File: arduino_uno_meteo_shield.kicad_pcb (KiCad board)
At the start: 2 copper layers, 13 parts

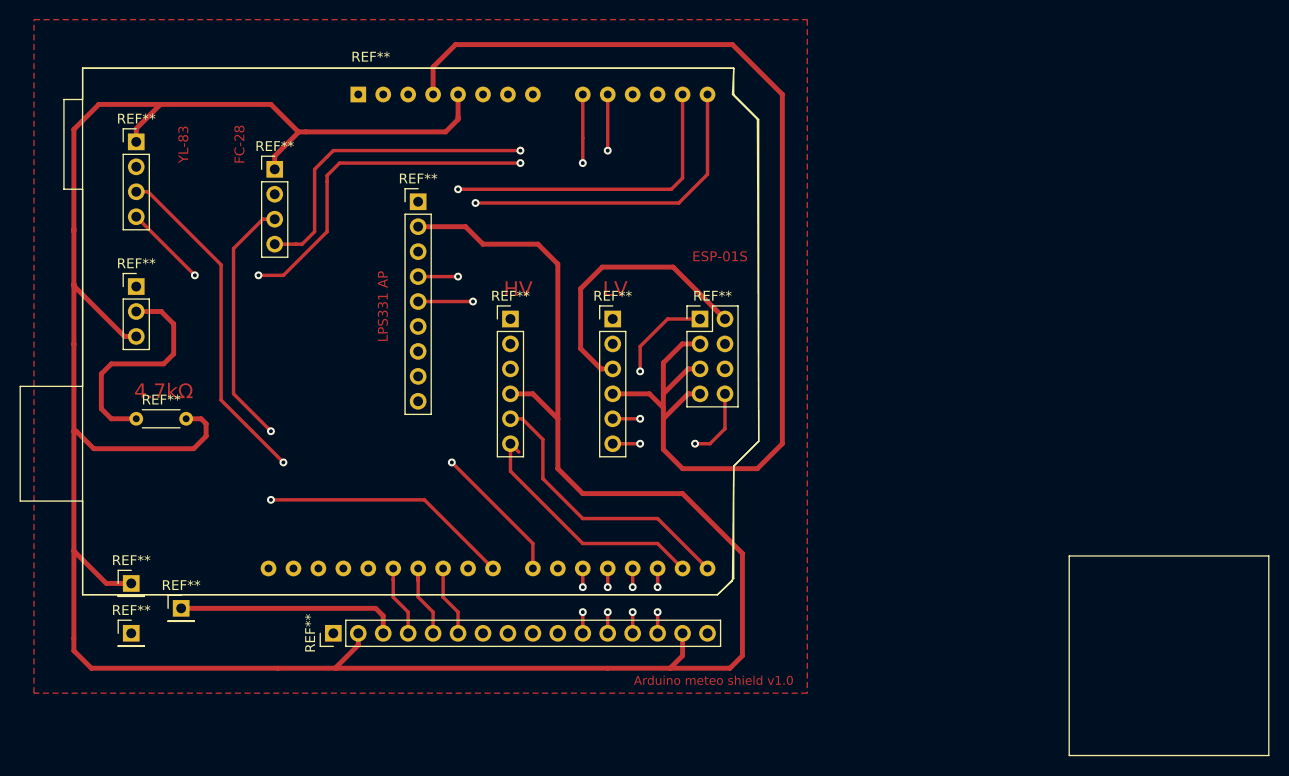
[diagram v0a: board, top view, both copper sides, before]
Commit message: make path wider
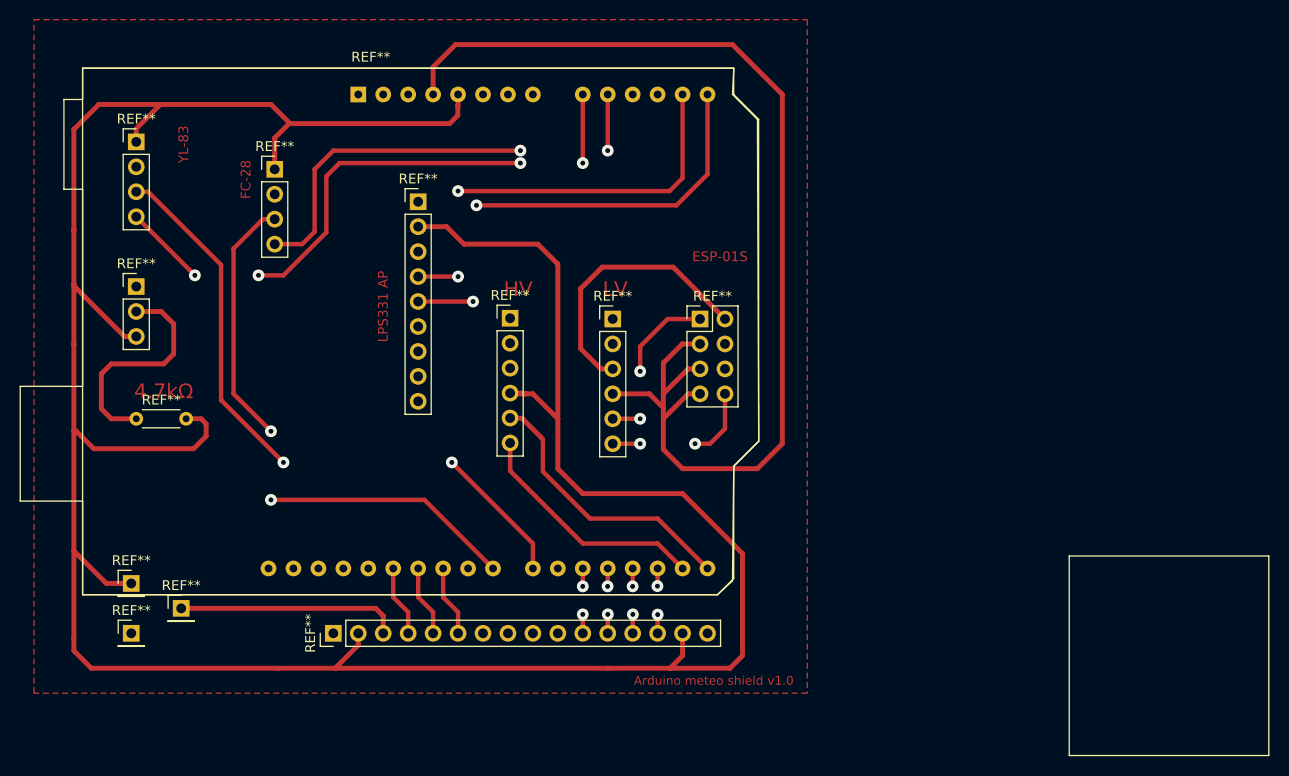
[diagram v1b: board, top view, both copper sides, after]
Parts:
- moved REF** 0.08 mm to (157.7, 88.8)
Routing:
- net (no net): track 870.0 -> 894.8 mm

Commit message: improving connections and add DTH11
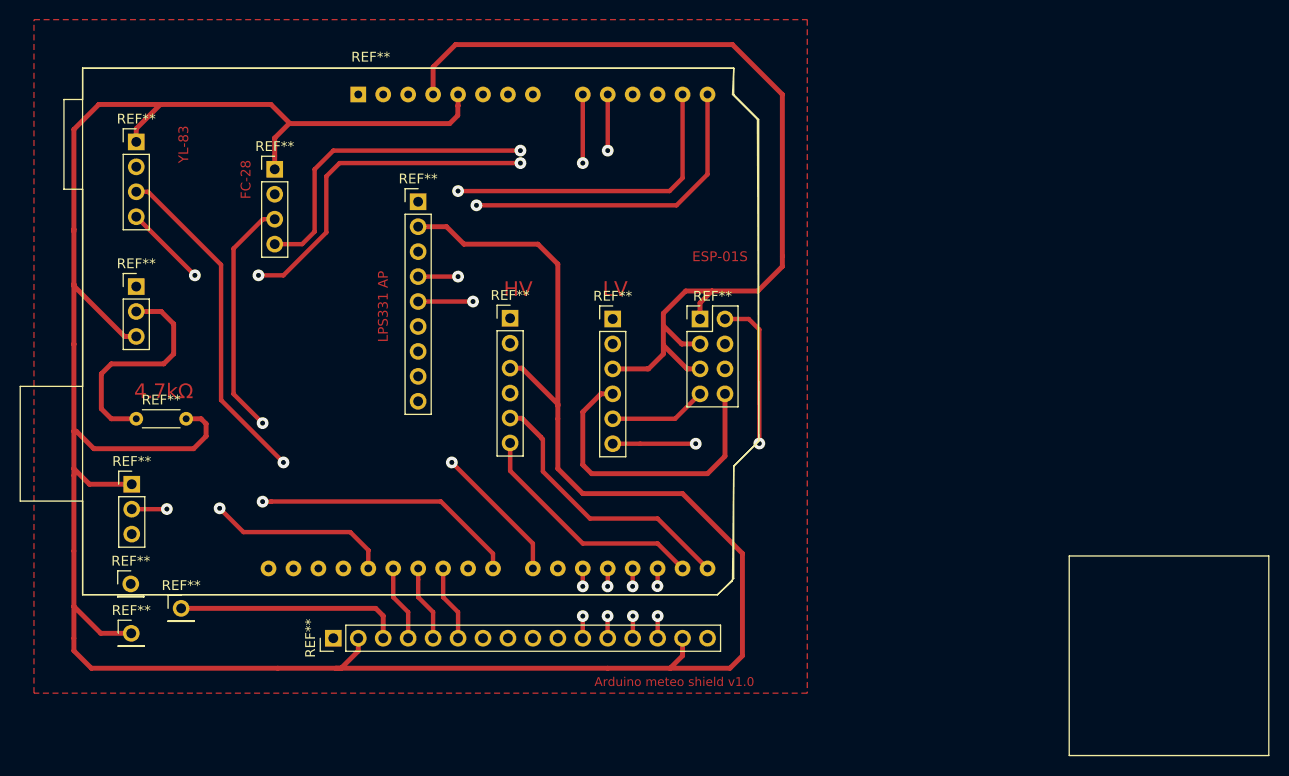
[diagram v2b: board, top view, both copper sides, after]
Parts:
- added REF**: PinHeader_1x03_P2.54mm_Vertical, Connector_PinHeader_2.54mm:PinHeader_1x03_P2.54mm_Vertical, F.Cu at (119.2, 105.7)
- moved REF** 0.50 mm to (139.7, 121.4)
- moved REF** 0.07 mm to (119.1, 115.9)
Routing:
- net (no net): track 894.8 -> 913.4 mm

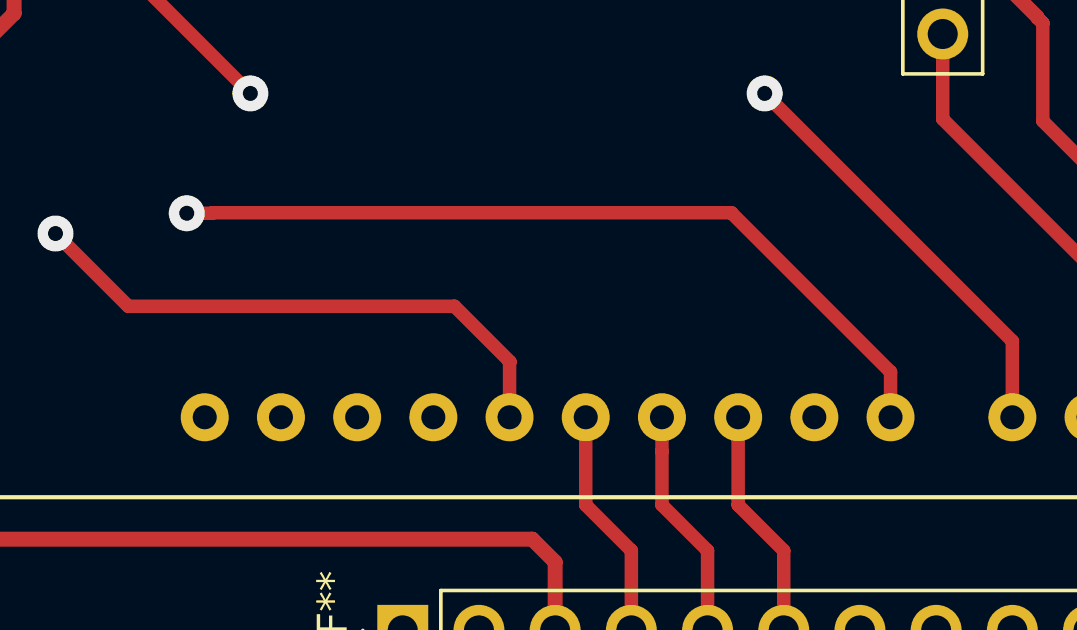
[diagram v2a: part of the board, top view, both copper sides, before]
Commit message: add holes for attachment
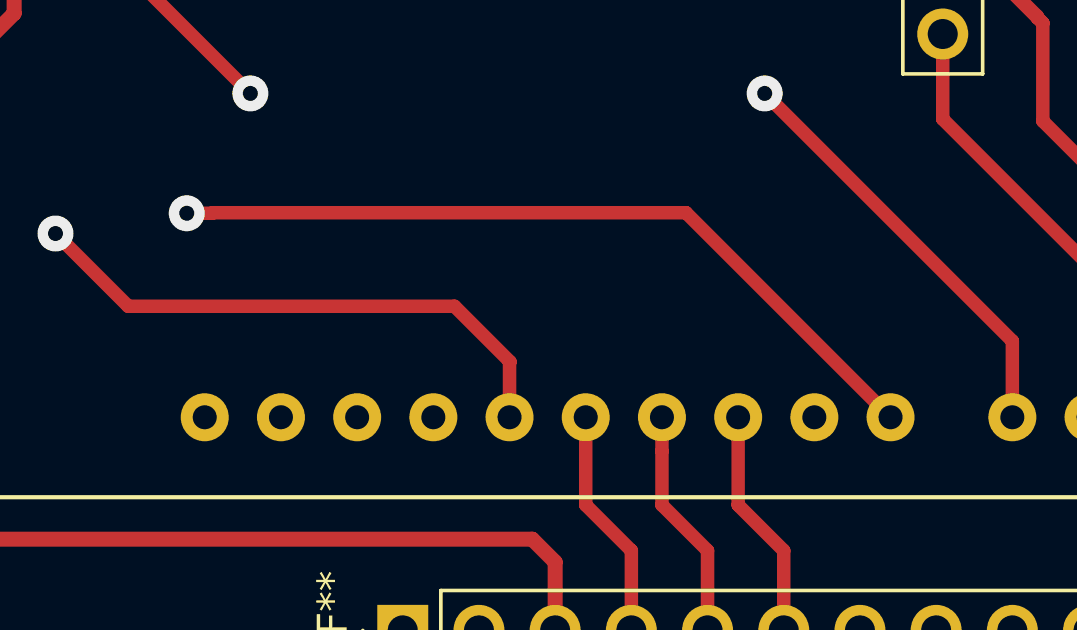
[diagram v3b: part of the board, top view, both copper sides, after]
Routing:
- net (no net): track 913.4 -> 912.5 mm
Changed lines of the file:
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@@
     (thickness 1.6)
     (drawings 21)
-    (tracks 241)
+    (tracks 240)
     (zones 0)
     (modules 14)
@@
   (segment (start 133.731 78.74) (end 132.528919 78.74) (width 0.45) (layer F.Cu) (net 0))
   (segment (start 132.528919 78.74) (end 129.54 81.728919) (width 0.45) (layer F.Cu) (net 0))
-  (segment (start 133.348528 107.5) (end 132.5 107.5) (width 0.45) (layer F.Cu) (net 0))
-  (segment (start 133.366028 107.4825) (end 133.348528 107.5) (width 0.45) (layer F.Cu) (net 0))
-  (segment (start 150.6525 107.4825) (end 133.366028 107.4825) (width 0.45) (layer F.Cu) (net 0))
-  (segment (start 155.96 114.3) (end 155.96 112.79) (width 0.45) (layer F.Cu) (net 0))
-  (segment (start 155.96 112.79) (end 150.6525 107.4825) (width 0.45) (layer F.Cu) (net 0))
+  (segment (start 133.366028 107.4825) (end 149.1425 107.4825) (width 0.45) (layer F.Cu) (net 0))
+  (segment (start 133.348528 107.5) (end 133.366028 107.4825) (width 0.45) (layer F.Cu) (net 0))
+  (segment (start 132.5 107.5) (end 133.348528 107.5) (width 0.45) (layer F.Cu) (net 0))
+  (segment (start 149.1425 107.4825) (end 155.96 114.3) (width 0.45) (layer F.Cu) (net 0))
   (zone (net 0) (net_name "") (layer F.Cu) (hatch edge 0.508)
     (connect_pads (clearance 0.508))
@@
       )
     )
+  )
+  (zone (net 0) (net_name "") (layer F.Cu) (hatch edge 0.508)
+    (connect_pads (clearance 0.508))
+    (min_thickness 0.254)
+    (keepout (tracks not_allowed) (vias not_allowed) (copperpour not_allowed))
+    (fill (arc_segments 32) (thermal_gap 0.508) (thermal_bridge_width 0.508))
+    (polygon
+      (pts
+        (xy 185.42 58.42) (xy 187.96 58.42) (xy 187.96 60.96) (xy 185.42 60.96)
+      )
+    )
+  )
+  (zone (net 0) (net_name "") (layer F.Cu) (hatch edge 0.508)
+    (connect_pads (clearance 0.508))
+    (min_thickness 0.254)
+    (keepout (tracks not_allowed) (vias not_allowed) (copperpour not_allowed))
+    (fill (arc_segments 32) (thermal_gap 0.508) (thermal_bridge_width 0.508))
+    (polygon
+      (pts
+        (xy 111.76 60.96) (xy 109.22 60.96) (xy 109.22 58.42) (xy 111.76 58.42)
+      )
+    )
+  )
+  (zone (net 0) (net_name "") (layer F.Cu) (hatch edge 0.508)
+    (connect_pads (clearance 0.508))
+    (min_thickness 0.254)
+    (keepout (tracks not_allowed) (vias not_allowed) (copperpour not_allowed))
+    (fill (arc_segments 32) (thermal_gap 0.508) (thermal_bridge_width 0.508))
+    (polygon
+      (pts
+        (xy 109.22 124.46) (xy 111.76 124.46) (xy 111.76 127) (xy 109.22 127)
+      )
+    )
+  )
+  (zone (net 0) (net_name "") (layer F.Cu) (hatch edge 0.508)
+    (connect_pads (clearance 0.508))
+    (min_thickness 0.254)
+    (keepout (tracks not_allowed) (vias not_allowed) (copperpour not_allowed))
+    (fill (arc_segments 32) (thermal_gap 0.508) (thermal_bridge_width 0.508))
+    (polygon
+      (pts
+        (xy 185.42 127) (xy 185.42 124.46) (xy 187.96 124.46) (xy 187.96 127)
+      )
+    )

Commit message: mirror fix
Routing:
- net (no net): track 912.5 -> 938.4 mm, vias 26 -> 32
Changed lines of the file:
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@@
     (thickness 1.6)
     (drawings 21)
-    (tracks 240)
+    (tracks 251)
     (zones 0)
     (modules 14)
@@
   (segment (start 133.731 72.31) (end 133.731 73.66) (width 0.5) (layer F.Cu) (net 0))
   (segment (start 133.35 67.056) (end 122.094 67.056) (width 0.5) (layer F.Cu) (net 0))
-  (segment (start 151.765 103.505) (end 151.765 103.505) (width 0.35) (layer F.Cu) (net 0))
-  (via (at 151.765 103.505) (size 1.2) (drill 0.5) (layers F.Cu B.Cu) (net 0))
-  (segment (start 134.62 103.505) (end 134.62 103.505) (width 0.35) (layer F.Cu) (net 0))
-  (via (at 134.62 103.505) (size 1.2) (drill 0.5) (layers F.Cu B.Cu) (net 0))
+  (via (at 140.716 104.14) (size 1.2) (drill 0.5) (layers F.Cu B.Cu) (net 0))
+  (via (at 134.62 104.14) (size 1.2) (drill 0.5) (layers F.Cu B.Cu) (net 0))
   (via (at 132.5 99.5) (size 1.2) (drill 0.5) (layers F.Cu B.Cu) (net 0))
   (via (at 132.5 107.5) (size 1.2) (drill 0.5) (layers F.Cu B.Cu) (net 0))
@@
   (via (at 170.2 119.15) (size 1.2) (drill 0.5) (layers F.Cu B.Cu) (net 0))
   (via (at 172.725 119.15) (size 1.2) (drill 0.5) (layers F.Cu B.Cu) (net 0))
-  (segment (start 148.34 114.3) (end 148.34 115.574) (width 0.35) (layer F.Cu) (net 0))
-  (segment (start 148.34 117.225) (end 148.34 115.574) (width 0.35) (layer F.Cu) (net 0))
   (segment (start 145.8 117.225) (end 145.8 115.43137) (width 0.35) (layer F.Cu) (net 0))
   (segment (start 158.75 71.755) (end 158.75 71.755) (width 0.35) (layer F.Cu) (net 0))
@@
   (via (at 165.1 73.025) (size 1.2) (drill 0.5) (layers F.Cu B.Cu) (net 0))
   (via (at 167.64 71.755) (size 1.2) (drill 0.5) (layers F.Cu B.Cu) (net 0))
-  (segment (start 119.634 75.946) (end 120.836081 75.946) (width 0.45) (layer F.Cu) (net 0))
-  (segment (start 120.836081 75.946) (end 128.27 83.379919) (width 0.45) (layer F.Cu) (net 0))
-  (segment (start 128.27 83.379919) (end 128.27 97.155) (width 0.45) (layer F.Cu) (net 0))
-  (segment (start 128.27 97.155) (end 134.62 103.505) (width 0.45) (layer F.Cu) (net 0))
   (segment (start 160.850541 100.93346) (end 160.850541 100.974459) (width 0.45) (layer F.Cu) (net 0))
   (segment (start 158.902081 98.985) (end 160.850541 100.93346) (width 0.45) (layer F.Cu) (net 0))
@@
   (segment (start 161.036 104.426) (end 165.83 109.22) (width 0.45) (layer F.Cu) (net 0))
   (segment (start 165.83 109.22) (end 172.72 109.22) (width 0.45) (layer F.Cu) (net 0))
-  (segment (start 151.765 103.505) (end 160.02 111.76) (width 0.45) (layer F.Cu) (net 0))
   (segment (start 160.02 111.76) (end 160.02 114.3) (width 0.45) (layer F.Cu) (net 0))
   (segment (start 145.8 114.3) (end 145.8 117.225) (width 0.45) (layer F.Cu) (net 0))
   (segment (start 147.32 118.745) (end 145.8 117.225) (width 0.45) (layer F.Cu) (net 0))
   (segment (start 147.32 120.904) (end 147.32 118.745) (width 0.45) (layer F.Cu) (net 0))
-  (segment (start 148.34 115.43137) (end 148.34 117.225) (width 0.45) (layer F.Cu) (net 0))
-  (segment (start 148.34 114.3) (end 148.34 115.43137) (width 0.45) (layer F.Cu) (net 0))
-  (segment (start 148.34 117.225) (end 149.86 118.745) (width 0.45) (layer F.Cu) (net 0))
-  (segment (start 149.86 118.745) (end 149.86 120.904) (width 0.45) (layer F.Cu) (net 0))
-  (segment (start 150.88 114.3) (end 150.88 117.225) (width 0.45) (layer F.Cu) (net 0))
   (segment (start 152.4 120.904) (end 152.4 118.745) (width 0.45) (layer F.Cu) (net 0))
-  (segment (start 152.4 118.745) (end 150.88 117.225) (width 0.45) (layer F.Cu) (net 0))
   (segment (start 165.1 114.3) (end 165.1 116.205) (width 0.45) (layer F.Cu) (net 0))
   (segment (start 167.64 114.3) (end 167.64 116.205) (width 0.45) (layer F.Cu) (net 0))
@@
   (segment (start 132.5 107.5) (end 133.348528 107.5) (width 0.45) (layer F.Cu) (net 0))
   (segment (start 149.1425 107.4825) (end 155.96 114.3) (width 0.45) (layer F.Cu) (net 0))
+  (segment (start 148.34 114.3) (end 148.34 115.43137) (width 0.45) (layer F.Cu) (net 0))
+  (segment (start 148.34 115.43137) (end 148.34 117.14626) (width 0.45) (layer F.Cu) (net 0))
+  (segment (start 152.4 118.745) (end 152.4 118.745) (width 0.45) (layer F.Cu) (net 0))
+  (via (at 152.4 118.745) (size 1.2) (drill 0.5) (layers F.Cu B.Cu) (net 0))
+  (segment (start 148.34 117.14626) (end 148.34 117.14626) (width 0.45) (layer F.Cu) (net 0))
+  (via (at 148.34 117.14626) (size 1.2) (drill 0.5) (layers F.Cu B.Cu) (net 0))
+  (via (at 125.476 87.884) (size 1.2) (drill 0.5) (layers F.Cu B.Cu) (net 0))
+  (segment (start 122.428 87.884) (end 122.174 88.138) (width 0.5) (layer F.Cu) (net 0))
+  (segment (start 125.476 87.884) (end 122.428 87.884) (width 0.5) (layer F.Cu) (net 0))
+  (via (at 141.732 87.884) (size 1.2) (drill 0.5) (layers F.Cu B.Cu) (net 0))
+  (segment (start 141.732 87.884) (end 141.732 99.568) (width 0.5) (layer F.Cu) (net 0))
+  (via (at 147.32 110.236) (size 1.2) (drill 0.5) (layers F.Cu B.Cu) (net 0))
+  (via (at 147.32 101.092) (size 1.2) (drill 0.5) (layers F.Cu B.Cu) (net 0))
+  (segment (start 150.88 113.796) (end 150.88 114.3) (width 0.5) (layer F.Cu) (net 0))
+  (segment (start 147.32 110.236) (end 150.88 113.796) (width 0.5) (layer F.Cu) (net 0))
+  (segment (start 141.732 99.568) (end 143.256 101.092) (width 0.5) (layer F.Cu) (net 0))
+  (segment (start 143.256 101.092) (end 147.32 101.092) (width 0.5) (layer F.Cu) (net 0))
+  (segment (start 120.836081 75.946) (end 119.634 75.946) (width 0.45) (layer F.Cu) (net 0))
+  (segment (start 128.27 83.379919) (end 120.836081 75.946) (width 0.45) (layer F.Cu) (net 0))
+  (segment (start 128.27 97.282) (end 128.27 83.379919) (width 0.45) (layer F.Cu) (net 0))
+  (segment (start 134.62 104.14) (end 134.020001 103.540001) (width 0.45) (layer F.Cu) (net 0))
+  (segment (start 140.716 104.14) (end 152.4 104.14) (width 0.45) (layer F.Cu) (net 0))
+  (segment (start 152.4 104.14) (end 160.02 111.76) (width 0.45) (layer F.Cu) (net 0))
+  (segment (start 132.588 102.108) (end 134.020001 103.540001) (width 0.45) (layer F.Cu) (net 0))
+  (segment (start 132.588 101.6) (end 132.588 102.108) (width 0.45) (layer F.Cu) (net 0))
+  (segment (start 132.588 101.6) (end 128.27 97.282) (width 0.45) (layer F.Cu) (net 0))
   (zone (net 0) (net_name "") (layer F.Cu) (hatch edge 0.508)
     (connect_pads (clearance 0.508))
